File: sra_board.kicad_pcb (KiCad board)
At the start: 2 copper layers, 90 x 89.5 mm, 200 parts, among them J1 Conn_01x14_Pin, J10 Conn_01x03_Pin, J11 Conn_01x03_Pin, J12 Conn_01x03_Pin, J13 MPU0650, J14 LSA, J15 OLED, J16 Conn_01x03_Pin, J17 Conn_01x03_Pin, J18 Conn_01x03_Pin, J3 Conn_01x08_Pin, J4 Conn_01x14_Pin, J5 USB_C_Receptacle_USB2.0_16P, J6 B2B-XH-A_LF__SN_, J7 B2B-XH-A_LF__SN_, J8 B2B-XH-A_LF__SN_, J9 Conn_01x03_Pin, Q1 SS8050, Q2 SS8050, Q3 AO3400A, Q4 AO3401A, Q5 AO3401A, Q6 AO3401A, Q7 AO3401A, SW1 SW_0, SW2 SW_EN, SW3 Switch, SW4 Switch, SW5 SW_Wuerth_450301014042, SW6 SW_Wuerth_450301014042, U1 MAX7219CWG_T, U2 CH340C, U3 TB6612FNG H-bridge Motor Driv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, U4 TPS54302, U5 CN3303, U7 ME6211C33M5, U8 ESP32-WROOM-32E

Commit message: Partial placing of components in PCB
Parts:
- removed 330: 330, Resistor_SMD:R_0805_2012Metric
- removed ? (x2): , 
- removed C22: 75pF, Capacitor_SMD:C_0805_2012Metric
- removed D76, D77: LED, LED_SMD:LED_0805_2012Metric
- removed G***: LOGO, logos:sra_logo_small_neg
- removed G*** (x2): LOGO, logos:sra_skull_big
- removed G***: LOGO, Logos:sra_logo_big
- removed G***: LOGO, logos:sra_board_github_qr_code
- removed G***: LOGO, logos:espressif_logo
- removed H5, H6: MountingHole, MountingHole:MountingHole_2.1mm
- removed J18: Conn_01x03_Pin, Connector_PinHeader_2.54mm:PinHeader_1x03_P2.54mm_Vertical
- removed JP2, JP3, JP4, JP5: SolderBridge, Connector_PinHeader_2.54mm:PinHeader_1x02_P2.54mm_Vertical
- removed Q6, Q7: AO3401A, Package_TO_SOT_SMD:SOT-23
- removed R50: 680, Resistor_SMD:R_0805_2012Metric
- removed SW5, SW6: SW_Wuerth_450301014042, Button_Switch_SMD:SW_SPDT_Shouhan_MSK12C02
- removed U8: ESP32-WROOM-32E, RF_Module:ESP32-WROOM-32D
- removed kibuzzard-658F2C3C: G***, kibuzzard-658F2C3C
- removed kibuzzard-668D4F81: G***, kibuzzard-668D4F81
- removed kibuzzard-668FE423: G***, kibuzzard-668FE423
- removed kibuzzard-668FF9B2: G***, kibuzzard-668FF9B2
- removed kibuzzard-66914CE9: G***, kibuzzard-66914CE9
- removed kibuzzard-66921043: G***, kibuzzard-66921043
- removed kibuzzard-66923428: G***, kibuzzard-66923428
- removed kibuzzard-66CD8CDE: G***, kibuzzard-66CD8CDE
- removed kibuzzard-66CD901B: G***, kibuzzard-66CD901B
- removed kibuzzard-66CF86D1: G***, kibuzzard-66CF86D1
- removed kibuzzard-66CF86E5: G***, kibuzzard-66CF86E5
- removed kibuzzard-66D06403: G***, kibuzzard-66D06403
- removed kibuzzard-66D06F4C: G***, kibuzzard-66D06F4C
- removed kibuzzard-66D06F54: G***, kibuzzard-66D06F54
- removed kibuzzard-66D58886: G***, kibuzzard-66D58886
- removed kibuzzard-675FD791: G***, kibuzzard-675FD791
- removed kibuzzard-675FDA6A: G***, kibuzzard-675FDA6A
- removed kibuzzard-675FF2F7: G***, kibuzzard-675FF2F7
- removed kibuzzard-675FF39E: G***, kibuzzard-675FF39E
- removed kibuzzard-6774F4AA: G***, kibuzzard-6774F4AA
- removed kibuzzard-6774F4AE: G***, kibuzzard-6774F4AE
- removed kibuzzard-67A02922: G***, kibuzzard-67A02922
- removed kibuzzard-68E7F907: G***, kibuzzard-68E7F907
- added C1: 0.1uF, Capacitor_SMD:C_0805_2012Metric, F.Cu at (202.5, 123.8)
- added C12: 0.1uF, Capacitor_SMD:C_0805_2012Metric, F.Cu at (119.1, 96.5)
- added C13: 22uF, Capacitor_SMD:C_0805_2012Metric, F.Cu at (119.1, 99.1)
- added C14: 10uF, Capacitor_SMD:C_1206_3216Metric, F.Cu at (302.6, 97.2)
- added C15: 0.1uF, Capacitor_SMD:C_1206_3216Metric, F.Cu at (307.0, 85.2)
- added D71: LED, LED_SMD:LED_0805_2012Metric, F.Cu at (73.8, 67.1)
- added D72: SS14, Diode_SMD:D_SMA, F.Cu at (123.6, 89.4)
- added H2: MountingHole, MountingHole:MountingHole_3.2mm_M3_DIN965_Pad, F.Cu at (44.1, 121.1)
- added H3: MountingHole, MountingHole:MountingHole_3.2mm_M3_DIN965_Pad, F.Cu at (127.8, 121.1)
- added J2: Conn_01x03_Pin, Connector_PinHeader_2.54mm:PinHeader_1x03_P2.54mm_Vertical, F.Cu at (178.7, 105.3)
- added U6: MAX7219CWG_T, footprints:SOIC24, F.Cu at (58.9, 91.1)
- C10, C11: footprint Capacitor_SMD:C_1206_3216Metric -> Capacitor_SMD:C_0805_2012Metric
- C17: value 1uf -> 10uF
- C18: value 1uf -> 0.1uF
- C19: value 0.1uf -> 22uF; footprint Capacitor_SMD:C_0805_2012Metric -> Capacitor_SMD:C_1206_3216Metric
- C2: value 0.1uF -> 22uF; footprint Capacitor_SMD:C_0805_2012Metric -> Capacitor_SMD:C_1206_3216Metric
- C21: value 22uF -> 75pF; footprint Capacitor_SMD:C_1206_3216Metric -> Capacitor_SMD:C_0805_2012Metric
- C3: value 0.1 uF -> 22uF; footprint Capacitor_SMD:C_0805_2012Metric -> Capacitor_SMD:C_1206_3216Metric
- C6: value 100nf -> 0.1uF
- C7: value 10uf -> 0.1uF
- C8, C9: value 22uF -> 0.1uF
- D1: value SP0503 -> LED; footprint Package_TO_SOT_SMD:SOT-143 -> LED_SMD:LED_0805_2012Metric
- D2: value SS34 -> LED; footprint Diode_SMD:D_SMB -> LED_SMD:LED_0805_2012Metric
- D3, D4: value LED -> SS34; footprint LED_SMD:LED_0805_2012Metric -> Diode_SMD:D_SMA
- D5: value LED -> SP0503; footprint LED_SMD:LED_0805_2012Metric -> Package_TO_SOT_SMD:SOT-143
- D6: value LED -> SS34; footprint LED_SMD:LED_0805_2012Metric -> Diode_SMD:D_SMB
- D68, D70: value SS34 -> LED; footprint Diode_SMD:D_SMA -> LED_SMD:LED_0805_2012Metric
- D75: value SS14 -> LED; footprint Diode_SMD:D_SMA -> LED_SMD:LED_0805_2012Metric
- F1: value 3A -> 1A
- F2: value 1A -> 3A
- H1, H4: footprint MountingHole:MountingHole_3.2mm_M3 -> MountingHole:MountingHole_3.2mm_M3_DIN965_Pad
- J1: value Conn_01x14_Pin -> Barrel_Jack; footprint Connector_PinHeader_2.54mm:PinHeader_1x10_P2.54mm_Vertical -> Connector_BarrelJack:BarrelJack_Wuerth_6941xx301002
- J10, J9: value Conn_01x03_Pin -> B2B-XH-A_LF__SN_; footprint Connector_PinHeader_2.54mm:PinHeader_1x03_P2.54mm_Vertical -> Connector_JST:JST_EH_B2B-EH-A_1x02_P2.50mm_Vertical
- J13: value MPU0650 -> Conn_01x03_Pin; footprint Connector_PinSocket_2.54mm:PinSocket_1x08_P2.54mm_Vertical -> Connector_PinHeader_2.54mm:PinHeader_1x03_P2.54mm_Vertical
- J14: value LSA -> MPU0650; footprint Connector_PinSocket_2.54mm:PinSocket_1x07_P2.54mm_Vertical -> Connector_PinSocket_2.54mm:PinSocket_1x08_P2.54mm_Vertical
- J15: value OLED -> Conn_01x03_Pin; footprint Connector_PinSocket_2.54mm:PinSocket_1x04_P2.54mm_Vertical -> Connector_PinHeader_2.54mm:PinHeader_1x03_P2.54mm_Vertical
- J16: value Conn_01x03_Pin -> LSA; footprint Connector_PinHeader_2.54mm:PinHeader_1x03_P2.54mm_Vertical -> Connector_FFC-FPC:JUSHUO_AFA07-S08FCA-00_1x8-1MP_P1.0mm_Horizontal
- J17: value Conn_01x03_Pin -> OLED; footprint Connector_PinHeader_2.54mm:PinHeader_1x03_P2.54mm_Vertical -> Connector_PinSocket_2.54mm:PinSocket_1x04_P2.54mm_Vertical
- J3: value Conn_01x08_Pin -> USB_C_Receptacle_USB2.0_16P; footprint Connector_PinHeader_2.54mm:PinHeader_1x10_P2.54mm_Vertical -> Connector_USB:USB_C_Receptacle_GCT_USB4105-xx-A_16P_TopMnt_Horizontal
- J5: value USB_C_Receptacle_USB2.0_16P -> Conn_01x03_Pin; footprint Connector_USB:USB_C_Receptacle_GCT_USB4105-xx-A_16P_TopMnt_Horizontal -> Connector_PinHeader_2.54mm:PinHeader_1x03_P2.54mm_Vertical
- J6: value B2B-XH-A_LF__SN_ -> Conn_01x08_Pin; footprint Connector_JST:JST_EH_B2B-EH-A_1x02_P2.50mm_Vertical -> Connector_PinHeader_2.54mm:PinHeader_1x10_P2.54mm_Vertical
- J7: value B2B-XH-A_LF__SN_ -> Conn_01x03_Pin; footprint Connector_JST:JST_EH_B2B-EH-A_1x02_P2.50mm_Vertical -> Connector_PinHeader_2.54mm:PinHeader_1x03_P2.54mm_Vertical
- J8: value B2B-XH-A_LF__SN_ -> Conn_01x14_Pin; footprint Connector_JST:JST_EH_B2B-EH-A_1x02_P2.50mm_Vertical -> Connector_PinHeader_2.54mm:PinHeader_1x10_P2.54mm_Vertical
- L2: footprint Inductor_SMD:L_Sunlord_MWSA1004S -> Inductor_SMD:L_Sunlord_MWSA0618S
- Q1: value SS8050 -> AO3400A
- Q2: value SS8050 -> AO3401A
- Q3: value AO3400A -> SS8050
- Q4: value AO3401A -> SS8050
- R1: value 100K -> 10k
- R10: value 5.1K -> 1k
- R11: value 5.1K -> 10K
- R12: value 100K -> 5.1K
- R13: value 40m -> 5.1K; footprint Resistor_SMD:R_1206_3216Metric -> Resistor_SMD:R_0805_2012Metric
- R14: value 1k -> 100K
- R15: value 1k -> 330
- R16: value 100k -> 10k
- R18: value 49.9 -> 105k
- R19: value 105k -> 4k7
- R2, R3, R8: value 10K -> 1k
- R20: value 330 -> 4k7
- R21: value 4k7 -> 13k3
- R22: value 4k7 -> 49.9
- R23: value 10k -> 100k
- R24: value 10k -> 330
- R25: value 13k3 -> 330
- R4: value 1k -> 40m; footprint Resistor_SMD:R_0805_2012Metric -> Resistor_SMD:R_1206_3216Metric
- R5, R6: value 1k -> 10K
- R9: value 100K -> 1k
- SW3, SW4: value Switch -> SW_Wuerth_450301014042; footprint Button_Switch_THT:SW_Push_2P2T_Toggle_CK_PVA2OAH5xxxxxxV2 -> Button_Switch_SMD:SW_SPDT_Shouhan_MSK12C02
- U1: value MAX7219CWG_T -> ESP32-WROOM-32E; footprint footprints:SOIC24 -> RF_Module:ESP32-WROOM-32D
- U2: value CH340C -> CN3303; footprint Package_SO:SOIC-16_3.9x9.9mm_P1.27mm -> easyeda2kicad:SOP-8_L4.9-W3.9-P1.27-LS6.0-BL
- U3: value TB6612FNG H-bridge Motor Driver -> CH340C; footprint footprints:MODULE_ROB-14450 -> Package_SO:SOIC-16_3.9x9.9mm_P1.27mm
- U4: value TPS54302 -> TB6612FNG H-bridge Motor Driver; footprint Package_TO_SOT_SMD:SOT-23-6 -> footprints:MODULE_ROB-14450
- U5: value CN3303 -> AMS1117-3.3; footprint easyeda2kicad:SOP-8_L4.9-W3.9-P1.27-LS6.0-BL -> Package_TO_SOT_SMD:SOT-223-3_TabPin2
- U7: value ME6211C33M5 -> TPS54302; footprint Package_TO_SOT_SMD:SOT-23-5 -> Package_TO_SOT_SMD:SOT-23-6
- moved U4 133.8 mm to (68.9, 113.2), turned to 0 degrees
- moved C8 132.0 mm to (64.1, 118.2), turned to 90 degrees
- moved D69 129.5 mm to (73.8, 77.6), turned to -135 degrees
- moved C9 128.1 mm to (64.1, 113.1)
- moved D67 127.0 mm to (73.8, 70.6), turned to -135 degrees
- moved R10 126.6 mm to (72.7, 117.2), turned to 0 degrees
- moved D70 124.3 mm to (73.8, 81.1), turned to -135 degrees
- moved R9 124.1 mm to (72.7, 114.3), turned to 0 degrees
- moved R16 122.0 mm to (315.2, 87.9), turned to 0 degrees
- moved J6 121.9 mm to (83.1, 79.0)
- moved J16 120.7 mm to (86.6, 119.3), turned to 0 degrees
- moved J15 119.5 mm to (54.7, 121.9), turned to -90 degrees
- moved D68 114.7 mm to (73.8, 74.1), turned to -135 degrees
- moved R25 104.4 mm to (110.3, 116.0), turned to 0 degrees
- moved J13 102.2 mm to (54.7, 114.4), turned to -90 degrees
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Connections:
- C10 pad 1: /VTPS -> /5V_P
- C11 pad 1: /VTPS -> /5V_P
- C16 pad 1: Net-(U4-BOOT) -> /5V_P
- C16 pad 2: Net-(U4-SW) -> GND
- C18 pad 1: /3V3 -> Net-(U7-BOOT)
- C18 pad 2: GND -> Net-(U7-SW)
- C19 pad 1: /EN -> +5V
- C2 pad 1: Net-(U2-V3) -> +BATT
- C21 pad 1: +5V -> Net-(C21-Pad1)
- C21 pad 2: GND -> Net-(U7-FB)
- C3 pad 1: /3V3 -> GND
- C3 pad 2: GND -> /5V_P_USB
- C4 pad 1: GND -> Net-(U3-V3)
- C4 pad 2: /0 -> GND
- C5 pad 1: GND -> /3V3
- C5 pad 2: /EN -> GND
- C6 pad 1: /5V_P -> GND
- C6 pad 2: GND -> /0
- C7 pad 1: /5V_P -> GND
- C7 pad 2: GND -> /EN
- C8 pad 1: GND -> /M2A
- C8 pad 2: /5V_P_USB -> /M2B
- C9 pad 1: +BATT -> /M1A
- C9 pad 2: GND -> /M1B
- D1 pad 2: /D+ -> Net-(D1-A)
- D10 pad 2: /R4 -> /R5
- D11 pad 1: /C2 -> /C1
- D11 pad 2: /R1 -> /R6
- D12 pad 1: /C2 -> /C1
- D12 pad 2: /R2 -> /R7
- D13 pad 1: /C2 -> /C1
- D13 pad 2: /R3 -> /R8
- D14 pad 1: /C2 -> /C1
- D14 pad 2: /R5 -> /R4
- D15 pad 2: /R6 -> /R1
- D16 pad 2: /R7 -> /R2
- D17 pad 2: /R8 -> /R3
- D18 pad 2: /R4 -> /R5
- D19 pad 1: /C3 -> /C2
- D19 pad 2: /R1 -> /R6
- D2 pad 1: /5V_P_USB -> Net-(D2-K)
- D2 pad 2: /VBUS -> Net-(D2-A)
- D20 pad 1: /C3 -> /C2
- D20 pad 2: /R2 -> /R7
- D21 pad 1: /C3 -> /C2
- D21 pad 2: /R3 -> /R8
- D22 pad 1: /C3 -> /C2
- D22 pad 2: /R5 -> /R4
- D23 pad 2: /R6 -> /R1
- D24 pad 2: /R7 -> /R2
- D25 pad 2: /R8 -> /R3
- D26 pad 2: /R4 -> /R5
- D27 pad 1: /C4 -> /C3
- D27 pad 2: /R1 -> /R6
- D28 pad 1: /C4 -> /C3
- D28 pad 2: /R2 -> /R7
- D29 pad 1: /C4 -> /C3
- D29 pad 2: /R3 -> /R8
- D3 pad 1: /C1 -> +BATT
- D3 pad 2: /R1 -> Net-(D3-A)
- D30 pad 1: /C4 -> /C3
- D30 pad 2: /R5 -> /R4
- D31 pad 2: /R6 -> /R1
- D32 pad 2: /R7 -> /R2
- D33 pad 2: /R8 -> /R3
- D34 pad 2: /R4 -> /R5
- D35 pad 1: /C5 -> /C4
- D35 pad 2: /R1 -> /R6
- D36 pad 1: /C5 -> /C4
- D36 pad 2: /R2 -> /R7
- D37 pad 1: /C5 -> /C4
- D37 pad 2: /R3 -> /R8
- D38 pad 1: /C5 -> /C4
- D38 pad 2: /R5 -> /R4
- D39 pad 2: /R6 -> /R1
- D4 pad 1: /C1 -> Net-(D4-K)
- D4 pad 2: /R2 -> GND
- D40 pad 2: /R7 -> /R2
- D41 pad 2: /R8 -> /R3
- D42 pad 2: /R4 -> /R5
- D43 pad 1: /C6 -> /C5
- D43 pad 2: /R1 -> /R6
- D44 pad 1: /C6 -> /C5
- D44 pad 2: /R2 -> /R7
- D45 pad 1: /C6 -> /C5
- D45 pad 2: /R3 -> /R8
- D46 pad 1: /C6 -> /C5
- D46 pad 2: /R5 -> /R4
- D47 pad 1: /C6 -> GND
- D47 pad 2: /R6 -> Net-(D47-A)
- D48 pad 2: /R7 -> /R1
- D49 pad 2: /R8 -> /R2
- D5 pad 1: /C1 -> GND
- D5 pad 2: /R3 -> /D-
- D50 pad 2: /R4 -> /R3
- D51 pad 1: /C7 -> /C6
- D51 pad 2: /R1 -> /R5
- D52 pad 1: /C7 -> /C6
- D52 pad 2: /R2 -> /R6
- D53 pad 1: /C7 -> /C6
- D53 pad 2: /R3 -> /R7
- D54 pad 1: /C7 -> /C6
- D54 pad 2: /R5 -> /R8
- D55 pad 1: /C7 -> /C6
- D55 pad 2: /R6 -> /R4
- D56 pad 2: /R7 -> /R1
- D57 pad 2: /R8 -> /R2
- D58 pad 2: /R4 -> /R3
- D59 pad 1: /C8 -> /C7
- D59 pad 2: /R1 -> /R5
- D6 pad 1: /C1 -> /5V_P_USB
- D6 pad 2: /R5 -> /VBUS
- D60 pad 1: /C8 -> /C7
- D60 pad 2: /R2 -> /R6
- D61 pad 1: /C8 -> /C7
- D61 pad 2: /R3 -> /R7
- D62 pad 1: /C8 -> /C7
- D62 pad 2: /R5 -> /R8
- D63 pad 1: /C8 -> /C7
- D63 pad 2: /R6 -> /R4
- D64 pad 2: /R7 -> /R1
- D65 pad 2: /R8 -> /R2
- D66 pad 2: /R4 -> /R3
- D67 pad 1: Net-(D67-K) -> /C8
- D67 pad 2: Net-(D67-A) -> /R5
- D68 pad 1: Net-(D68-K) -> /C8
- D68 pad 2: GND -> /R6
- D69 pad 1: GND -> /C8
- D69 pad 2: Net-(D69-A) -> /R7
- D7 pad 2: /R6 -> /R1
- D70 pad 1: +BATT -> /C8
- D70 pad 2: Net-(D70-A) -> /R8
- D74 pad 2: /12V -> /5V_P
- D75 pad 1: /5V_P_USB -> Net-(D75-K)
- D75 pad 2: +5V -> /12V
- D8 pad 2: /R7 -> /R2
- D9 pad 2: /R8 -> /R3
- F1 pad 1: Net-(D73-K) -> /5V_P_USB
- F1 pad 2: /12V_Switch -> Net-(SW3-B)
- F2 pad 1: /5V_P_USB -> Net-(D73-K)
- F2 pad 2: /5V_Switch -> Net-(SW4-B)
- J1 pad 1: GND -> +BATT
- J1 pad 2: /3V3 -> GND
- J1 pad 3: /EN -> (no net)
- J10 pad 1: /15 -> /M2A
- J10 pad 2: /5V_P -> /M2B
- J11 pad 1: /33 -> /27
- J12 pad 1: /19 -> /15
- J13 pad 1: /3V3 -> /33
- J13 pad 2: GND -> /5V_P
- J13 pad 3: /21 -> GND
- J14 pad 1: /32 -> /3V3
- J14 pad 2: /35 -> GND
- J14 pad 3: /34 -> /21
- J14 pad 4: /39 -> /22
- J14 pad 5: /36 -> unconnected-(J14-Pin_5-Pad5)
- J14 pad 6: GND -> unconnected-(J14-Pin_6-Pad6)
- J14 pad 7: /3V3 -> unconnected-(J14-Pin_7-Pad7)
- J15 pad 1: GND -> /19
- J15 pad 2: /3V3 -> /5V_P
- J15 pad 3: /21 -> GND
- J16 pad 1: /5V_P -> /3V3
- J16 pad 2: /5V_P -> GND
- J16 pad 3: /5V_P -> /36
- J17 pad 1: /3V3 -> GND
- J17 pad 3: /3V3 -> /21
- J4 pad 10: /17 -> /25
- J4 pad 2: /23 -> /3V3
- J4 pad 3: /22 -> /EN
- J4 pad 4: /TXD -> /36
- J4 pad 5: /RXD -> /39
- J4 pad 6: /21 -> /34
- J4 pad 7: /19 -> /35
- J4 pad 8: /18 -> /32
- J4 pad 9: /5 -> /33
- J6 pad 1: GND -> /12
- J6 pad 2: +BATT -> /14
- J7 pad 1: /M1A -> GND
- J7 pad 2: /M1B -> GND
- J8 pad 1: /M2A -> GND
- J8 pad 2: /M2B -> /23
- J9 pad 1: /27 -> /M1A
- J9 pad 2: /5V_P -> /M1B
- L1 pad 1: Net-(D70-A) -> Net-(D3-A)
- L1 pad 2: Net-(D68-K) -> Net-(D4-K)
- L2 pad 1: Net-(U4-SW) -> Net-(U7-SW)
- Q1 pad 1: Net-(Q1-Pad1) -> /LDRV
- Q1 pad 2: /~{RTS} -> GND
- Q1 pad 3: /EN -> Net-(D3-A)
- Q2 pad 1: Net-(Q2-Pad1) -> Net-(Q2-G)
- Q2 pad 2: /~{DTR} -> /CSN
- Q2 pad 3: /0 -> Net-(D4-K)
- Q3 pad 1: /LDRV -> Net-(Q3-Pad1)
- Q3 pad 2: GND -> /~{RTS}
- Q3 pad 3: Net-(D70-A) -> /EN
- Q4 pad 1: Net-(Q4-G) -> Net-(Q4-Pad1)
- Q4 pad 2: /CSN -> /~{DTR}
- Q4 pad 3: Net-(D68-K) -> /0
- R1 pad 1: /5V_P_USB -> /3V3
- R1 pad 2: GND -> /EN
- R10 pad 1: Net-(J5-CC1) -> /26
- R10 pad 2: GND -> Net-(U4-BI2)
- R11 pad 1: Net-(J5-CC2) -> /0
- R11 pad 2: GND -> /3V3
- R12 pad 1: Net-(Q7-G) -> Net-(J3-CC1)
- R12 pad 2: Net-(JP4-A) -> GND
- R13 pad 1: /CSN -> Net-(J3-CC2)
- R13 pad 2: /5V_P_USB -> GND
- R14 pad 1: Net-(D67-A) -> /5V_P_USB
- R14 pad 2: /5V_P_USB -> GND
- R15 pad 1: Net-(D69-A) -> /3V3
- R15 pad 2: Net-(D67-K) -> Net-(D47-A)
- R16 pad 1: Net-(C22-Pad1) -> /3V3
- R16 pad 2: Net-(U4-FB) -> Net-(U6-ISET)
- R17 pad 1: Net-(U4-EN) -> Net-(U7-EN)
- R18 pad 1: +5V -> GND
- R18 pad 2: Net-(C22-Pad1) -> Net-(U7-EN)
- R19 pad 1: GND -> /3V3
- R19 pad 2: Net-(U4-EN) -> /21
- R2 pad 1: /~{DTR} -> Net-(D1-A)
- R2 pad 2: Net-(Q1-Pad1) -> Net-(D2-K)
- R20 pad 1: GND -> /3V3
- R20 pad 2: Net-(D76-K) -> /22
- R21 pad 1: /3V3 -> Net-(U7-FB)
- R21 pad 2: /21 -> GND
- R22 pad 1: /3V3 -> +5V
- R22 pad 2: /22 -> Net-(C21-Pad1)
- R23 pad 1: /3V3 -> Net-(C21-Pad1)
- R23 pad 2: /EN -> Net-(U7-FB)
- R24 pad 1: /3V3 -> GND
- R24 pad 2: Net-(U1-ISET) -> Net-(D74-K)
- R25 pad 1: Net-(U4-FB) -> GND
- R25 pad 2: GND -> Net-(D75-K)
- R3 pad 1: /~{RTS} -> Net-(D2-A)
- R3 pad 2: Net-(Q2-Pad1) -> /5V_P_USB
- R4 pad 1: /12 -> /CSN
- R4 pad 2: Net-(U3-AI1) -> /5V_P_USB
- R5 pad 1: /13 -> /~{DTR}
- R5 pad 2: Net-(U3-AI2) -> Net-(Q3-Pad1)
- R6 pad 1: /25 -> /~{RTS}
- R6 pad 2: Net-(U3-BI1) -> Net-(Q4-Pad1)
- R7 pad 1: /26 -> /12
- R7 pad 2: Net-(U3-BI2) -> Net-(U4-AI1)
- R8 pad 1: /0 -> /13
- R8 pad 2: /3V3 -> Net-(U4-AI2)
- R9 pad 1: Net-(Q6-G) -> /25
- R9 pad 2: Net-(JP3-A) -> Net-(U4-BI1)
- SW3 pad 1: unconnected-(SW3-A-Pad1) -> Net-(SW3-B)
- SW3 pad 2: Net-(JP2-B) -> unconnected-(SW3-C-Pad2)
- SW3 pad 3: /12V -> /5V_P
- SW4 pad 1: unconnected-(SW4-A-Pad1) -> Net-(SW4-B)
- SW4 pad 2: Net-(JP5-B) -> unconnected-(SW4-C-Pad2)
- SW4 pad 3: /5V_P -> /12V
- U1 pad 1: /23 -> GND
- U1 pad 10: /C6 -> /25
- U1 pad 11: /C2 -> /26
- U1 pad 12: /5 -> /27
- U1 pad 13: /18 -> /14
- U1 pad 14: /R2 -> /12
- U1 pad 15: /R7 -> GND
- U1 pad 16: /R3 -> /13
- U1 pad 17: /R8 -> unconnected-(U1-NC-Pad17)
- U1 pad 18: Net-(U1-ISET) -> unconnected-(U1-NC-Pad18)
- U1 pad 19: /5V_P -> unconnected-(U1-NC-Pad19)
- U1 pad 2: /C1 -> /3V3
- U1 pad 20: /R4 -> unconnected-(U1-NC-Pad20)
- U1 pad 21: /R6 -> unconnected-(U1-NC-Pad21)
- U1 pad 22: /R1 -> unconnected-(U1-NC-Pad22)
- U1 pad 23: /R5 -> /15
- U1 pad 24: unconnected-(U1-DOUT-Pad24) -> /2
- U1 pad 3: /C5 -> /EN
- U1 pad 4: GND -> /36
- U1 pad 5: /C7 -> /39
- U1 pad 6: /C3 -> /34
- U1 pad 7: /C4 -> /35
- U1 pad 8: /C8 -> /32
- U1 pad 9: GND -> /33
- U2 pad 1: GND -> Net-(D2-K)
- U2 pad 2: /RXD -> /5V_P_USB
- U2 pad 3: /TXD -> +BATT
- U2 pad 4: Net-(U2-V3) -> GND
- U2 pad 5: /D+ -> /LDRV
- U2 pad 6: /D- -> Net-(Q2-G)
- U2 pad 7: unconnected-(U2-NC-Pad7) -> /5V_P_USB
- U2 pad 8: unconnected-(U2-NC-Pad8) -> /CSN
- U3 pad 1: /12V -> GND
- U3 pad 10: /3V3 -> unconnected-(U3-~{DSR}-Pad10)
- U3 pad 11: Net-(U3-BI2) -> unconnected-(U3-~{RI}-Pad11)
- U3 pad 12: Net-(U3-BI1) -> unconnected-(U3-~{DCD}-Pad12)
- U3 pad 13: /3V3 -> /~{DTR}
- U3 pad 14: Net-(U3-AI1) -> /~{RTS}
- U3 pad 15: Net-(U3-AI2) -> unconnected-(U3-R232-Pad15)
- U3 pad 2: /3V3 -> /RXD
- U3 pad 3: GND -> /TXD
- U3 pad 4: /M1A -> Net-(U3-V3)
- U3 pad 5: /M1B -> /D+
- U3 pad 6: /M2B -> /D-
- U3 pad 7: /M2A -> unconnected-(U3-NC-Pad7)
- U3 pad 8: GND -> unconnected-(U3-NC-Pad8)
- U3 pad 9: GND -> unconnected-(U3-~{CTS}-Pad9)
- U4 pad 1: GND -> /12V
- U4 pad 2: Net-(U4-SW) -> /3V3
- U4 pad 3: /VTPS -> GND
- U4 pad 4: Net-(U4-FB) -> /M1A
- U4 pad 5: Net-(U4-EN) -> /M1B
- U4 pad 6: Net-(U4-BOOT) -> /M2B
- U5 pad 1: Net-(D67-K) -> GND
- U5 pad 2: /5V_P_USB -> /3V3
- U5 pad 3: +BATT -> /5V_P
- U7 pad 1: /5V_P -> GND
- U7 pad 2: GND -> Net-(U7-SW)
- U7 pad 3: /5V_P -> /VTPS
- U7 pad 4: unconnected-(U7-NC-Pad4) -> Net-(U7-FB)
- U7 pad 5: /3V3 -> Net-(U7-EN)
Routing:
- net /3V3: track 266.9 -> 0.00 mm, vias 4 -> 0
- net /5V_P: track 197.7 -> 0.00 mm, vias 2 -> 0
- net /12V: track 115.2 -> 0.00 mm, vias 2 -> 0
- net /0: track 93.6 -> 0.00 mm, vias 1 -> 0
- net /5V_P_USB: track 90.1 -> 0.00 mm
- net /22: track 86.9 -> 0.00 mm
- net /19: track 75.5 -> 0.00 mm, vias 1 -> 0
- net /D+: track 67.1 -> 0.00 mm, vias 3 -> 0
- net /D-: track 67.0 -> 0.00 mm, vias 3 -> 0
- net /21: track 63.3 -> 0.00 mm
- net /C1: track 63.1 -> 0.00 mm, vias 2 -> 0
- net /C2: track 63.1 -> 0.00 mm, vias 5 -> 0
- net /C3: track 63.0 -> 0.00 mm, vias 5 -> 0
- net /TXD: track 61.9 -> 0.00 mm, vias 2 -> 0
- net /R2: track 61.8 -> 0.00 mm
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- removed copper zone on B.Cu, net +BATT
- removed copper zone on F.Cu, net +BATT
- removed copper zone on F.Cu, net /5V_P
- removed copper zone on F.Cu, net /VTPS
- removed copper zone on B.Cu, net GND
- removed copper zone on F.Cu, net GND
- removed copper zone on F.Cu, net Net-(Q7-G)
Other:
- board size 90 x 89.5 mm -> 90 x 70 mm
- board text removed: "0"
- board text removed: "0.1 uF"
- board text removed: "0.1uF"
- board text removed: "0.1uf"
- board text removed: "100K"
- board text removed: "100k"
- board text removed: "100nf"
- board text removed: "105k"
- board text removed: "10K"
- board text removed: "10k"
- board text removed: "10uF"
- board text removed: "10uH"
- board text removed: "10uf"
- board text removed: "12"
- board text removed: "13"
- board text removed: "13k3"
- board text removed: "14"
- board text removed: "15"
- board text removed: "16"
- board text removed: "17"
- board text removed: "18"
- board text removed: "19"
- board text removed: "1A"
- board text removed: "1k"
- board text removed: "1uf"
- board text removed: "2"
- board text removed: "21"
- board text removed: "22"
- board text removed: "22uF"
- board text removed: "23"
- board text removed: "25"
- board text removed: "26"
- board text removed: "27"
- board text removed: "32"
- board text removed: "33"
- board text removed: "330"
- board text removed: "34"
- board text removed: "35"
- board text removed: "36"
- board text removed: "39"
- board text removed: "3A"
- board text removed: "4"
- board text removed: "4.7uH"
- board text removed: "40m"
- board text removed: "49.9"
- board text removed: "4k7"
- board text removed: "5"
- board text removed: "5.1K"
- board text removed: "511k"
- board text removed: "680"
- board text removed: "75pF"
- board text removed: "Buck converter circuit"
- board text removed: "CN3303"
- board text removed: "CN3303 circuit"
- board text removed: "EN"
- board text removed: "GND"
- board text removed: "GND 3V3"
- board text removed: "IN1"
- board text removed: "IN2"
- board text removed: "IN3"
- board text removed: "IN4"
- board text removed: "LED"
- board text removed: "M1A"
- board text removed: "M1B"
- board text removed: "M2A"
- board text removed: "M2B"
- board text removed: "MAX7219"
- board text removed: "ME6211"
- board text removed: "NMOS"
- board text removed: "PCB Edge"
- board text removed: "PMOS"
- board text removed: "PWM1"
- board text removed: "PWM2"
- board text removed: "RXD"
- board text removed: "SP0503"
- board text removed: "SS14"
- board text removed: "SS34"
- board text removed: "SS8050"
- board text removed: "STBY"
- board text removed: "Switch 12v"
- board text removed: "Switch 5v"
- board text removed: "TPS"
- board text removed: "TXD"
- board text removed: "USB circuit"
- board text removed: "VCC"
- board text removed: "VM"
- board text removed: "sravjti.in"

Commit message: Partial routing complete
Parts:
- removed JP1: SolderBridge, Connector_PinHeader_2.54mm:PinHeader_1x02_P2.54mm_Vertical
- removed Q5: AO3401A, Package_TO_SOT_SMD:SOT-23
- removed R14: 100K, Resistor_SMD:R_0805_2012Metric
- added H5: MountingHole, MountingHole:MountingHole_2.1mm, F.Cu at (79.0, 95.2)
- added H6: MountingHole, MountingHole:MountingHole_2.1mm, F.Cu at (93.9, 95.1)
- H1, H2, H3, H4: footprint MountingHole:MountingHole_3.2mm_M3_DIN965_Pad -> MountingHole:MountingHole_3.2mm_M3_DIN965
- moved R16 257.5 mm to (58.0, 99.8), turned to 90 degrees
- moved C15 206.3 mm to (100.8, 91.5), turned to 180 degrees
- moved C14 202.0 mm to (100.8, 88.1), turned to 180 degrees
- moved J7 146.2 mm to (42.9, 85.9), turned to 90 degrees
- moved J5 141.2 mm to (42.9, 89.8), turned to 90 degrees
- moved R20 138.2 mm to (90.9, 88.0), turned to 90 degrees
- moved J2 136.2 mm to (42.9, 93.7), turned to 90 degrees
- moved R19 134.4 mm to (93.8, 88.0), turned to 90 degrees
- moved C11 128.8 mm to (81.4, 104.3), turned to 90 degrees
- moved C10 127.3 mm to (81.4, 108.7), turned to -90 degrees
- moved J17 125.1 mm to (87.7, 99.8), turned to 90 degrees
- moved R15 124.9 mm to (95.5, 108.5), turned to -90 degrees
- moved U5 111.1 mm to (87.2, 108.7), turned to -90 degrees
- moved R1 99.9 mm to (124.5, 78.4), turned to -90 degrees
- moved R11 99.1 mm to (111.8, 78.4), turned to 90 degrees
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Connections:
- C14 pad 1: /VTPS -> /12V
- C15 pad 1: /VTPS -> /12V
- D5 pad 2: /D- -> /D+
- D5 pad 3: /D+ -> /D-
- F1 pad 2: Net-(SW3-B) -> Net-(SW3-C)
- F2 pad 2: Net-(SW4-B) -> Net-(SW4-C)
- J16 pad 1: /3V3 -> unconnected-(J16-Pin_1-Pad1)
- J16 pad 2: GND -> /3V3
- J16 pad 3: /36 -> GND
- J16 pad 4: /39 -> /36
- J16 pad 5: /34 -> /39
- J16 pad 6: /35 -> /34
- J16 pad 7: /32 -> /35
- J16 pad 8: unconnected-(J16-Pin_8-Pad8) -> /32
- R17 pad 2: /VTPS -> /12V
- SW3 pad 1: Net-(SW3-B) -> unconnected-(SW3-B-Pad1)
- SW3 pad 2: unconnected-(SW3-C-Pad2) -> Net-(SW3-C)
- SW4 pad 1: Net-(SW4-B) -> unconnected-(SW4-B-Pad1)
- SW4 pad 2: unconnected-(SW4-C-Pad2) -> Net-(SW4-C)
- U7 pad 3: /VTPS -> /12V
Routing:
- net /3V3: track 0.00 -> 195.9 mm, vias 0 -> 3
- net /5V_P: track 0.00 -> 134.6 mm, vias 0 -> 7
- net /12V: track 0.00 -> 124.6 mm, vias 0 -> 7
- net /EN: track 0.00 -> 91.2 mm, vias 0 -> 1
- net /18: track 0.00 -> 81.9 mm, vias 0 -> 3
- net /5: track 0.00 -> 81.0 mm, vias 0 -> 3
- net /23: track 0.00 -> 78.6 mm, vias 0 -> 3
- net /36: track 0.00 -> 66.4 mm, vias 0 -> 1
- net /34: track 0.00 -> 64.7 mm, vias 0 -> 1
- net /5V_P_USB: track 0.00 -> 64.6 mm, vias 0 -> 8
- net /39: track 0.00 -> 64.5 mm, vias 0 -> 1
- net /R2: track 0.00 -> 64.2 mm
- net /R1: track 0.00 -> 64.0 mm, vias 0 -> 2
- net /35: track 0.00 -> 63.1 mm, vias 0 -> 1
- net /32: track 0.00 -> 62.2 mm, vias 0 -> 2
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- added copper zone on F.Cu, net +BATT
- added copper zone on B.Cu, net /12V
- added copper zone on F.Cu, net /12V
- added copper zone on B.Cu, net /5V_P_USB
- added copper zone on F.Cu, net /VBUS
- added copper zone on B.Cu, net GND
- added copper zone on F.Cu, net GND
- added copper zone on F.Cu, net Net-(D3-A)

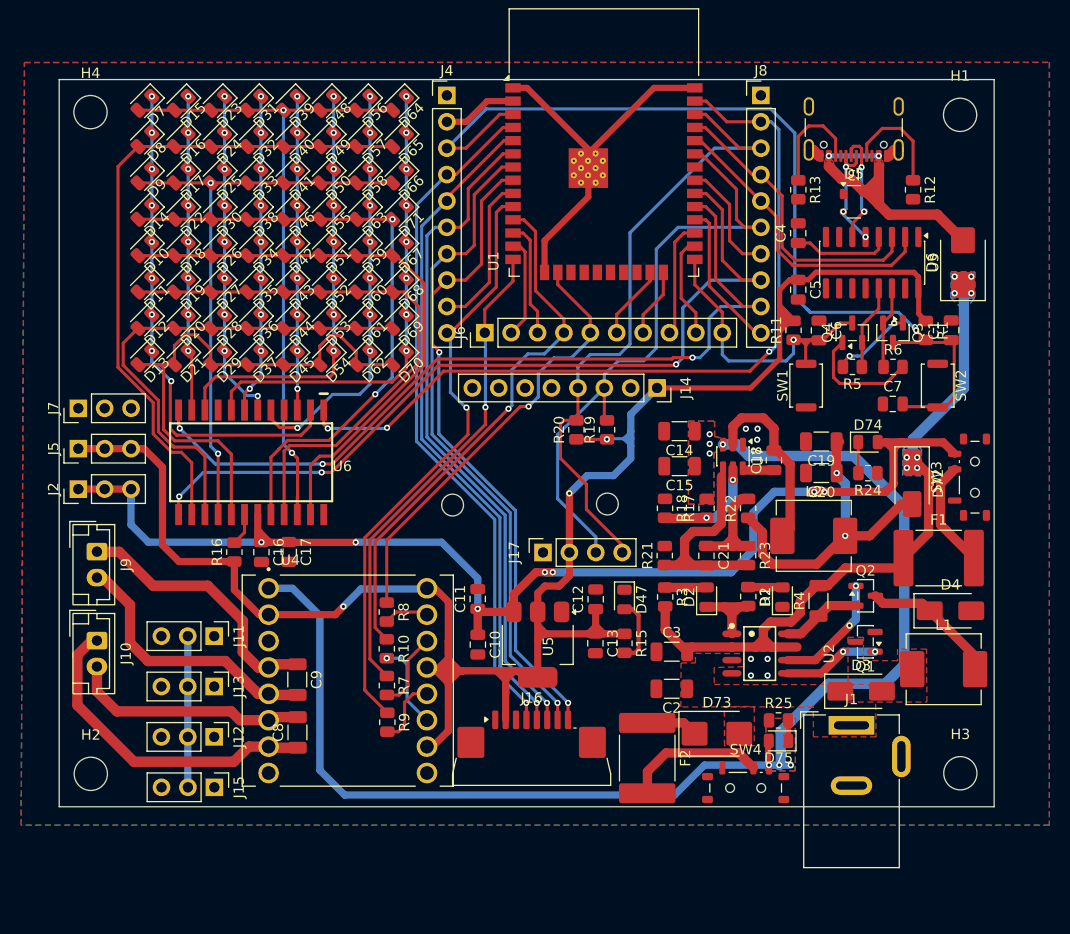
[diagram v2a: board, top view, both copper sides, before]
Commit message: Adding new layout of pcb
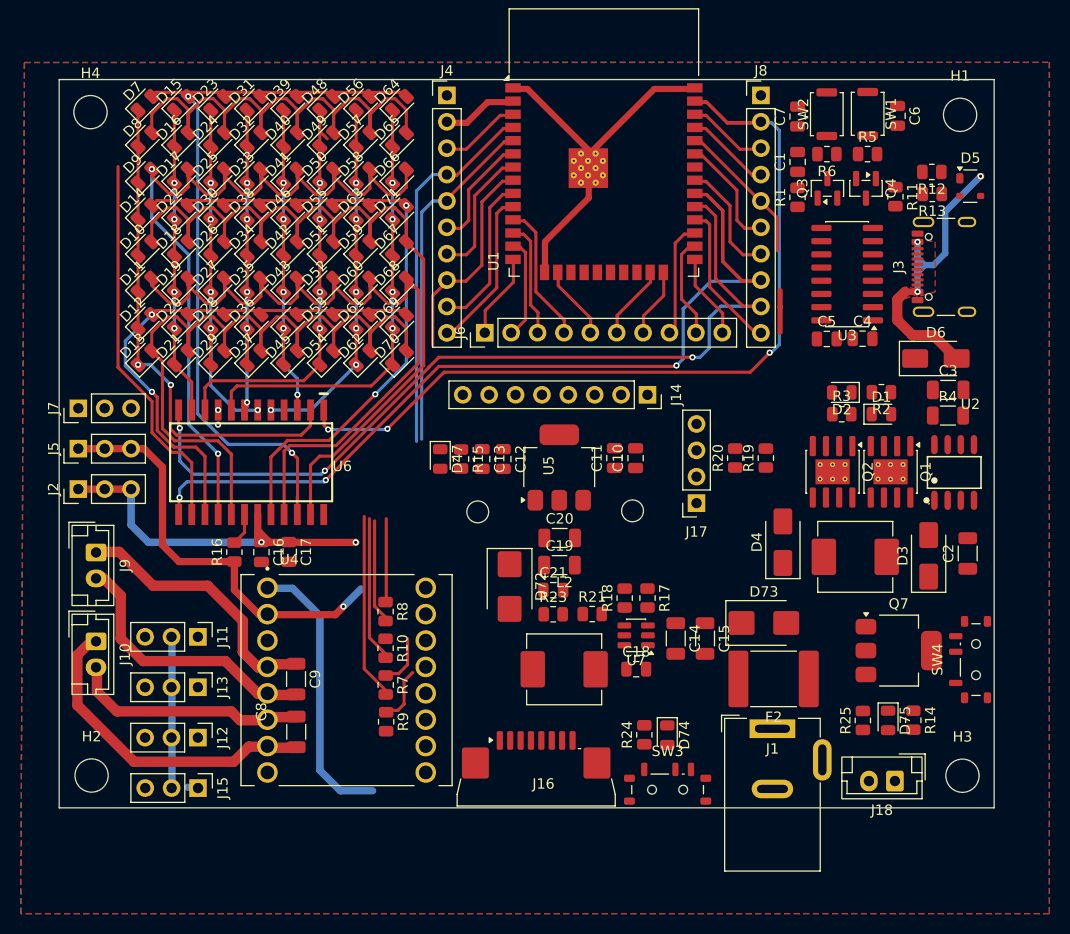
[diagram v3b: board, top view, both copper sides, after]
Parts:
- removed F1: 1A, Fuse:Fuse_2920_7451Metric
- removed R22: 49.9, Resistor_SMD:R_0805_2012Metric
- added J18: B2B-XH-A_LF__SN_, Connector_JST:JST_EH_B2B-EH-A_1x02_P2.50mm_Vertical, F.Cu at (121.5, 121.8)
- added Q7: ZXMP4A16GTA, Package_TO_SOT_SMD:SOT-223, F.Cu at (121.9, 109.2)
- added R14: 100K, Resistor_SMD:R_0805_2012Metric, F.Cu at (123.3, 115.9)
- C21: value 75pF -> NC
- D3, D4: value SS34 -> SS54
- D6: value SS34 -> SS54; footprint Diode_SMD:D_SMB -> Diode_SMD:D_SMA
- D72: value SS14 -> SS34; footprint Diode_SMD:D_SMA -> Diode_SMD:D_SMB
- L1: value 4.7uH -> 6.8uH
- L2: footprint Inductor_SMD:L_Sunlord_MWSA0618S -> Inductor_SMD:L_Sunlord_MWSA0603S
- Q1: value AO3400A -> DMN3016lss; footprint Package_TO_SOT_SMD:SOT-23 -> Package_SO:SOIC-8-1EP_3.9x4.9mm_P1.27mm_EP2.41x3.3mm_ThermalVias
- Q2: value AO3401A -> SI4435FDY; footprint Package_TO_SOT_SMD:SOT-23 -> Package_SO:SOIC-8-1EP_3.9x4.9mm_P1.27mm_EP2.41x3.3mm_ThermalVias
- R17: value 511k -> 10K
- R18: value 105k -> 4k7
- moved SW3 42.2 mm to (99.7, 122.6), turned to 0 degrees
- moved D72 40.0 mm to (84.4, 103.1)
- moved C3 36.6 mm to (126.7, 84.2)
- moved D74 34.2 mm to (99.6, 117.4), turned to -90 degrees
- moved R24 33.1 mm to (97.4, 117.4), turned to 90 degrees
- moved C2 31.3 mm to (128.5, 99.9), turned to 90 degrees
- moved C7 29.1 mm to (112.2, 57.8), turned to 90 degrees
- moved SW2 28.2 mm to (115.0, 57.6), turned to 90 degrees
- moved C19 27.9 mm to (89.3, 101.0), turned to 0 degrees
- moved L2 27.2 mm to (89.7, 111.0), turned to 180 degrees
- moved SW1 26.8 mm to (118.9, 57.6), turned to -90 degrees
- moved C20 26.0 mm to (89.3, 98.4), turned to 0 degrees
- moved U2 25.6 mm to (127.2, 92.1), turned to 0 degrees
- moved SW4 25.4 mm to (129.3, 110.1), turned to 90 degrees
- moved R3 24.5 mm to (116.4, 86.5), turned to 0 degrees
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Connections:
- C19 pad 1: +5V -> Net-(D72-A)
- C20 pad 1: +5V -> Net-(D72-A)
- C21 pad 1: Net-(C21-Pad1) -> Net-(D72-A)
- D6 pad 1: /5V_P_USB -> /5V_P
- D72 pad 1: /5V_P_USB -> /5V_P
- D72 pad 2: +5V -> Net-(D72-A)
- F2 pad 1: Net-(D73-K) -> Net-(Q7-S)
- F2 pad 2: Net-(SW4-C) -> Net-(D73-K)
- L2 pad 2: +5V -> Net-(D72-A)
- R17 pad 1: Net-(U7-EN) -> /EN
- R18 pad 2: Net-(U7-EN) -> /EN
- R23 pad 1: Net-(C21-Pad1) -> Net-(D72-A)
- SW3 pad 1: unconnected-(SW3-B-Pad1) -> /EN
- SW3 pad 2: Net-(SW3-C) -> GND
- SW3 pad 3: /5V_P -> unconnected-(SW3-A-Pad3)
- SW4 pad 1: unconnected-(SW4-B-Pad1) -> Net-(Q7-G)
- SW4 pad 2: Net-(SW4-C) -> GND
- SW4 pad 3: /12V -> unconnected-(SW4-A-Pad3)
- U7 pad 5: Net-(U7-EN) -> /EN
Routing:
- net /3V3: track 195.9 -> 52.0 mm, vias 3 -> 1
- net /12V: track 124.6 -> 26.8 mm, vias 7 -> 0
- net /5V_P: track 134.6 -> 51.0 mm, vias 7 -> 2
- net /EN: track 91.2 -> 7.72 mm, vias 1 -> 0
- net /5V_P_USB: track 64.6 -> 0.00 mm, vias 8 -> 0
- net /22: track 62.1 -> 7.72 mm
- net /34: track 64.7 -> 11.0 mm, vias 1 -> 0
- net /35: track 63.1 -> 12.7 mm, vias 1 -> 0
- net /21: track 61.4 -> 11.0 mm
- net /32: track 62.2 -> 20.7 mm, vias 2 -> 0
- net /26: track 52.0 -> 13.5 mm, vias 1 -> 0
- net /25: track 57.7 -> 20.6 mm, vias 1 -> 0
- net /R5: track 56.1 -> 92.0 mm
- net /12: track 46.5 -> 13.1 mm, vias 1 -> 0
- net /R2: track 64.2 -> 96.9 mm
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- removed copper zone on F.Cu, net +BATT
- removed copper zone on B.Cu, net /12V
- removed copper zone on F.Cu, net /12V
- removed copper zone on B.Cu, net /5V_P_USB
- removed copper zone on F.Cu, net Net-(D3-A)
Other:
- board size 90 x 70 mm -> 90 x 70.1 mm
